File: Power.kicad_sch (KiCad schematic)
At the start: 18 parts, among them U1 LP5907MFX-1.8, U4 TLV75525PDBV, U7 LP5907MFX-1.2

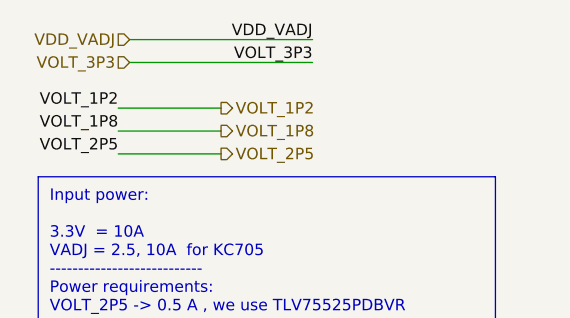
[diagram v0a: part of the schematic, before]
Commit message: DRC, ERC OK
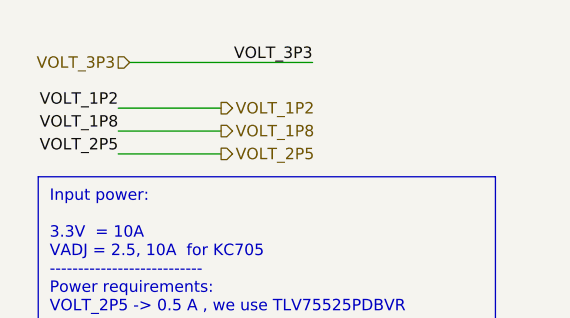
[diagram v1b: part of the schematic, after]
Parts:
- D2, D3, D4: footprint Diodes_SMD:D_SOD-523 -> SODFL1608X70N
- R16, R17, R8: symbol FMC_MIPI_v2-rescue:R-Device -> FMC_MIPI_v2:R
- U1: footprint TO_SOT_Packages_SMD:SOT-23-5 -> Package_TO_SOT_SMD:SOT-23-5; symbol FMC_MIPI_v2-rescue:LP5907MFX-1.8-Regulator_Linear -> FMC_MIPI_v2:LP5907MFX-1.8-Regulator_Linear
- U4: symbol FMC_MIPI_v2-rescue:TLV75525PDBV-Regulator_Linear -> FMC_MIPI_v2:TLV75525PDBV-Regulator_Linear
- U7: footprint TO_SOT_Packages_SMD:SOT-23-5 -> Package_TO_SOT_SMD:SOT-23-5; symbol FMC_MIPI_v2-rescue:LP5907MFX-1.2-Regulator_Linear -> FMC_MIPI_v2:LP5907MFX-1.2-Regulator_Linear
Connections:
- removed net Earth: C25.1, C26.1, C27.1, C28.1, C29.1, C30.1, C31.1, C7.1, C8.1, D2.2, D3.2, D4.2, U1.2 (GND), U4.2 (GND), U7.2 (GND)
- new net: C26.1, C31.1, D4.2
- new net: C29.1, C8.1, D2.2
- new net: C28.1, C30.1, D3.2
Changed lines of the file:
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@@
-    (stroke (width 0) (type default) (color 0 0 0 0))
-  )
-  (wire (pts (xy 45.72 13.97) (xy 25.4 13.97))
     (stroke (width 0) (type default) (color 0 0 0 0))
   )
@@
     (effects (font (size 1.27 1.27)) (justify right bottom))
   )
-  (label "VDD_VADJ" (at 45.72 13.97 180)
-    (effects (font (size 1.27 1.27)) (justify right bottom))
-  )
   (label "VOLT_1P2" (at 101.6 137.16 180)
     (effects (font (size 1.27 1.27)) (justify right bottom))
@@
     (effects (font (size 1.27 1.27)) (justify left))
   )
-  (hierarchical_label "VDD_VADJ" (shape input) (at 25.4 13.97 180)
-    (effects (font (size 1.27 1.27)) (justify right))
-  )
   (hierarchical_label "VOLT_3P3" (shape input) (at 25.4 16.51 180)
     (effects (font (size 1.27 1.27)) (justify right))
@@
       (effects (font (size 1.27 1.27)) (justify left) hide)
     )
-    (property "Footprint" "Diodes_SMD:D_SOD-523" (id 2) (at 96.52 76.2 0)
+    (property "Footprint" "SODFL1608X70N" (id 2) (at 96.52 76.2 0)
       (effects (font (size 1.27 1.27)) (justify left bottom) hide)
     )
@@
       (effects (font (size 1.27 1.27)) (justify left) hide)
     )
-    (property "Footprint" "Diodes_SMD:D_SOD-523" (id 2) (at 93.98 109.22 0)
+    (property "Footprint" "SODFL1608X70N" (id 2) (at 93.98 109.22 0)
       (effects (font (size 1.27 1.27)) (justify left bottom) hide)
     )
@@
       (effects (font (size 1.27 1.27)) (justify left) hide)
     )
-    (property "Footprint" "Diodes_SMD:D_SOD-523" (id 2) (at 93.98 147.32 0)
+    (property "Footprint" "SODFL1608X70N" (id 2) (at 93.98 147.32 0)
       (effects (font (size 1.27 1.27)) (justify left bottom) hide)
     )
@@
     (pin "2")
   )
-  (symbol (lib_id "FMC_MIPI_v2-rescue:Earth-power") (at 54.61 80.01 0) (unit 1)
+  (symbol (lib_id "FMC_MIPI_v2:Earth") (at 54.61 80.01 0) (unit 1)
     (in_bom yes) (on_board yes)
     (property "Reference" "#PWR0149" (id 0) (at 54.61 86.36 0)
@@
     (pin "2")
   )
-  (symbol (lib_id "FMC_MIPI_v2-rescue:Earth-power") (at 34.29 80.01 0) (unit 1)
+  (symbol (lib_id "FMC_MIPI_v2:Earth") (at 34.29 80.01 0) (unit 1)
     (in_bom yes) (on_board yes)
     (property "Reference" "#PWR0150" (id 0) (at 34.29 86.36 0)
@@
     (pin "1")
   )
-  (symbol (lib_id "FMC_MIPI_v2-rescue:Earth-power") (at 68.58 83.82 0) (unit 1)
+  (symbol (lib_id "FMC_MIPI_v2:Earth") (at 68.58 83.82 0) (unit 1)
     (in_bom yes) (on_board yes)
     (property "Reference" "#PWR0151" (id 0) (at 68.58 90.17 0)
@@
     (pin "1")
   )
-  (symbol (lib_id "FMC_MIPI_v2-rescue:R-Device") (at 39.37 72.39 0) (mirror y) (unit 1)
+  (symbol (lib_id "FMC_MIPI_v2:R") (at 39.37 72.39 0) (mirror y) (unit 1)
     (in_bom yes) (on_board yes)
     (property "Reference" "R16" (id 0) (at 41.91 72.39 90))
@@
     (pin "2")
   )
-  (symbol (lib_id "FMC_MIPI_v2-rescue:TLV75525PDBV-Regulator_Linear") (at 54.61 68.58 0) (unit 1)
+  (symbol (lib_id "FMC_MIPI_v2:TLV75525PDBV-Regulator_Linear") (at 54.61 68.58 0) (unit 1)
     (in_bom yes) (on_board yes)
     (property "Reference" "U4" (id 0) (at 54.61 59.8932 0))
@@
     (pin "5")
   )
-  (symbol (lib_id "FMC_MIPI_v2-rescue:LP5907MFX-1.8-Regulator_Linear") (at 54.61 101.6 0) (unit 1)
+  (symbol (lib_id "FMC_MIPI_v2:LP5907MFX-1.8-Regulator_Linear") (at 54.61 101.6 0) (unit 1)
     (in_bom yes) (on_board yes)
     (property "Reference" "U1" (id 0) (at 54.61 92.2782 0))
     (property "Value" "LP5907MFX-1.8" (id 1) (at 54.61 94.5896 0))
-    (property "Footprint" "TO_SOT_Packages_SMD:SOT-23-5" (id 2) (at 54.61 92.71 0)
+    (property "Footprint" "Package_TO_SOT_SMD:SOT-23-5" (id 2) (at 54.61 92.71 0)
       (effects (font (size 1.27 1.27)) hide)
     )
@@
     (pin "5")
   )
-  (symbol (lib_id "FMC_MIPI_v2-rescue:Earth-power") (at 54.61 113.03 0) (unit 1)
+  (symbol (lib_id "FMC_MIPI_v2:Earth") (at 54.61 113.03 0) (unit 1)
     (in_bom yes) (on_board yes)
     (property "Reference" "#PWR0134" (id 0) (at 54.61 119.38 0)
@@
     (pin "2")
   )
-  (symbol (lib_id "FMC_MIPI_v2-rescue:Earth-power") (at 34.29 113.03 0) (unit 1)
+  (symbol (lib_id "FMC_MIPI_v2:Earth") (at 34.29 113.03 0) (unit 1)
     (in_bom yes) (on_board yes)
     (property "Reference" "#PWR0135" (id 0) (at 34.29 119.38 0)
@@
     (pin "1")
   )
-  (symbol (lib_id "FMC_MIPI_v2-rescue:Earth-power") (at 68.58 116.84 0) (unit 1)
+  (symbol (lib_id "FMC_MIPI_v2:Earth") (at 68.58 116.84 0) (unit 1)
     (in_bom yes) (on_board yes)
     (property "Reference" "#PWR0136" (id 0) (at 68.58 123.19 0)
@@
     (pin "1")
   )
-  (symbol (lib_id "FMC_MIPI_v2-rescue:R-Device") (at 39.37 105.41 0) (mirror y) (unit 1)
+  (symbol (lib_id "FMC_MIPI_v2:R") (at 39.37 105.41 0) (mirror y) (unit 1)
     (in_bom yes) (on_board yes)
     (property "Reference" "R8" (id 0) (at 41.91 105.41 90))
@@
     (pin "2")
   )
-  (symbol (lib_id "FMC_MIPI_v2-rescue:LP5907MFX-1.2-Regulator_Linear") (at 54.61 139.7 0) (unit 1)
+  (symbol (lib_id "FMC_MIPI_v2:LP5907MFX-1.2-Regulator_Linear") (at 54.61 139.7 0) (unit 1)
     (in_bom yes) (on_board yes)
     (property "Reference" "U7" (id 0) (at 54.61 130.3782 0))
     (property "Value" "LP5907MFX-1.2" (id 1) (at 54.61 132.6896 0))
-    (property "Footprint" "TO_SOT_Packages_SMD:SOT-23-5" (id 2) (at 54.61 130.81 0)
+    (property "Footprint" "Package_TO_SOT_SMD:SOT-23-5" (id 2) (at 54.61 130.81 0)
       (effects (font (size 1.27 1.27)) hide)
     )
@@
     (pin "5")
   )
-  (symbol (lib_id "FMC_MIPI_v2-rescue:Earth-power") (at 54.61 152.4 0) (unit 1)
+  (symbol (lib_id "FMC_MIPI_v2:Earth") (at 54.61 152.4 0) (unit 1)
     (in_bom yes) (on_board yes)
     (property "Reference" "#PWR0152" (id 0) (at 54.61 158.75 0)
@@
     (pin "2")
   )
-  (symbol (lib_id "FMC_MIPI_v2-rescue:Earth-power") (at 34.29 151.13 0) (unit 1)
+  (symbol (lib_id "FMC_MIPI_v2:Earth") (at 34.29 151.13 0) (unit 1)
     (in_bom yes) (on_board yes)
     (property "Reference" "#PWR0153" (id 0) (at 34.29 157.48 0)
@@
     (pin "1")
   )
-  (symbol (lib_id "FMC_MIPI_v2-rescue:Earth-power") (at 68.58 154.94 0) (unit 1)
+  (symbol (lib_id "FMC_MIPI_v2:Earth") (at 68.58 154.94 0) (unit 1)
     (in_bom yes) (on_board yes)
     (property "Reference" "#PWR0154" (id 0) (at 68.58 161.29 0)
@@
     (pin "1")
   )
-  (symbol (lib_id "FMC_MIPI_v2-rescue:R-Device") (at 39.37 143.51 0) (mirror y) (unit 1)
+  (symbol (lib_id "FMC_MIPI_v2:R") (at 39.37 143.51 0) (mirror y) (unit 1)
     (in_bom yes) (on_board yes)
     (property "Reference" "R17" (id 0) (at 41.91 143.51 90))

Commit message: All warnings fixed
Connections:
- net Earth: now reaches C26.1, C31.1, D4.2
- net Earth: now also C25.1, C27.1, C28.1, C29.1, C30.1, C7.1, C8.1, D2.2, D3.2, U1.2 (GND), U4.2 (GND), U7.2 (GND)

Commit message: JLCPCB BOM OK
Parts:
- C29: LCSC (none) -> C1779; Part Number C2012X7R1H475K125AC -> CL21A475KAQNNNE
- C7: LCSC (none) -> C28323; Part Number UMK212B7105KG-T -> CL21B105KBFNNNE
- D2, D3, D4: LCSC (none) -> C117557
- R16, R17, R8: LCSC (none) -> C17477; Part Number RC0805JR-070RL -> 0805W8F0000T5E
- U1: LCSC (none) -> C92498; Part Number (none) -> LP5907MFX-1.8/NOPB; Part number LP5907MFX-1.8/NOPB -> (none)
- U4: LCSC (none) -> NeedToAsk
- U7: LCSC (none) -> C73478
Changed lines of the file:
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@@
       (effects (font (size 1.27 1.27)) (justify left bottom) hide)
+    )
+    (property "LCSC" "C117557" (id 10) (at 92.71 66.04 90)
+      (effects (font (size 1.27 1.27)) hide)
     )
     (pin "1")
@@
       (effects (font (size 1.27 1.27)) (justify left bottom) hide)
     )
+    (property "LCSC" "C117557" (id 10) (at 90.17 99.06 90)
+      (effects (font (size 1.27 1.27)) hide)
+    )
     (pin "1")
     (pin "2")
@@
       (effects (font (size 1.27 1.27)) hide)
     )
-    (property "Datasheet" "https://www.mouser.com/ProductDetail/TDK/C2012X7R1H475K125AC?qs=P1JMDcb91o6brNyz9C%252BI3w%3D%3D" (id 3) (at 80.01 104.14 0)
-      (effects (font (size 1.27 1.27)) hide)
-    )
-    (property "Part Number" "C2012X7R1H475K125AC" (id 4) (at 80.01 104.14 0)
+    (property "Datasheet" "https://www.mouser.com/ProductDetail/Samsung-Electro-Mechanics/CL21A475KAQNNNE?qs=yOVawPpwOwkWIBpK%2Fbg0Aw%3D%3D" (id 3) (at 80.01 104.14 0)
+      (effects (font (size 1.27 1.27)) hide)
+    )
+    (property "Part Number" "CL21A475KAQNNNE" (id 4) (at 80.01 104.14 0)
       (effects (font (size 1.27 1.27)) hide)
     )
@@
     )
     (property "Voltage" "25V" (id 6) (at 80.01 104.14 0)
+      (effects (font (size 1.27 1.27)) hide)
+    )
+    (property "LCSC" "C1779" (id 7) (at 80.01 104.14 0)
       (effects (font (size 1.27 1.27)) hide)
     )
@@
     (property "Manufacturer_Part_Number" "UCLAMP0501H.TCT" (id 9) (at 76.2 147.32 0)
       (effects (font (size 1.27 1.27)) (justify left bottom) hide)
+    )
+    (property "LCSC" "C117557" (id 10) (at 90.17 137.16 90)
+      (effects (font (size 1.27 1.27)) hide)
     )
     (pin "1")
@@
       (effects (font (size 1.27 1.27)) hide)
     )
-    (property "Datasheet" "https://www.mouser.com/ProductDetail/YAGEO/RC0805JR-070RL?qs=3ldFlDWnkKyEhdaPjQHEFA%3D%3D" (id 3) (at 39.37 72.39 0)
+    (property "Datasheet" "https://www.mouser.com/ProductDetail/Royalohm/0805W8F0000T5E?qs=e8oIoAS2J1TZ0ecBNS6tzg%3D%3D" (id 3) (at 39.37 72.39 0)
       (effects (font (size 1.27 1.27)) hide)
     )
@@
       (effects (font (size 1.524 1.524)) hide)
     )
-    (property "Part Number" "RC0805JR-070RL" (id 6) (at 39.37 72.39 90)
-      (effects (font (size 1.524 1.524)) hide)
+    (property "Part Number" "0805W8F0000T5E" (id 6) (at 39.37 72.39 90)
+      (effects (font (size 1.524 1.524)) hide)
+    )
+    (property "LCSC" "C17477" (id 7) (at 388.62 198.12 90)
+      (effects (font (size 1.27 1.27)) hide)
     )
     (pin "1")
@@
       (effects (font (size 1.27 1.27)) hide)
     )
+    (property "LCSC" "NeedToAsk" (id 4) (at 54.61 68.58 0)
+      (effects (font (size 1.27 1.27)) hide)
+    )
     (pin "1")
     (pin "2")
@@
       (effects (font (size 1.27 1.27)) hide)
     )
-    (property "Part number" "LP5907MFX-1.8/NOPB" (id 4) (at 54.61 101.6 0)
+    (property "Part Number" "LP5907MFX-1.8/NOPB" (id 4) (at 54.61 101.6 0)
+      (effects (font (size 1.27 1.27)) hide)
+    )
+    (property "LCSC" "C92498" (id 5) (at 54.61 101.6 0)
       (effects (font (size 1.27 1.27)) hide)
     )
@@
       (effects (font (size 1.27 1.27)) hide)
     )
-    (property "Datasheet" "https://www.mouser.com/ProductDetail/Taiyo-Yuden/UMK212B7105KG-T?qs=PzICbMaShUdi76GLXMVYcA%3D%3D" (id 3) (at 34.29 106.68 0)
-      (effects (font (size 1.27 1.27)) hide)
-    )
-    (property "Part Number" "UMK212B7105KG-T" (id 4) (at 34.29 106.68 0)
+    (property "Datasheet" "https://www.mouser.com/ProductDetail/Samsung-Electro-Mechanics/CL21B105KBFNNNE?qs=yOVawPpwOwmddQEBPU6Y9A%3D%3D" (id 3) (at 34.29 106.68 0)
+      (effects (font (size 1.27 1.27)) hide)
+    )
+    (property "Part Number" "CL21B105KBFNNNE" (id 4) (at 34.29 106.68 0)
       (effects (font (size 1.27 1.27)) hide)
     )
@@
     )
     (property "Voltage" "50 VDC" (id 6) (at 34.29 106.68 0)
+      (effects (font (size 1.27 1.27)) hide)
+    )
+    (property "LCSC" "C28323" (id 7) (at 34.29 106.68 0)
       (effects (font (size 1.27 1.27)) hide)
     )
@@
       (effects (font (size 1.27 1.27)) hide)
     )
-    (property "Datasheet" "https://www.mouser.com/ProductDetail/YAGEO/RC0805JR-070RL?qs=3ldFlDWnkKyEhdaPjQHEFA%3D%3D" (id 3) (at 39.37 105.41 0)
+    (property "Datasheet" "https://www.mouser.com/ProductDetail/Royalohm/0805W8F0000T5E?qs=e8oIoAS2J1TZ0ecBNS6tzg%3D%3D" (id 3) (at 39.37 105.41 0)
       (effects (font (size 1.27 1.27)) hide)
     )
@@
       (effects (font (size 1.524 1.524)) hide)
     )
-    (property "Part Number" "RC0805JR-070RL" (id 6) (at 39.37 105.41 90)
-      (effects (font (size 1.524 1.524)) hide)
+    (property "Part Number" "0805W8F0000T5E" (id 6) (at 39.37 105.41 90)
+      (effects (font (size 1.524 1.524)) hide)
+    )
+    (property "LCSC" "C17477" (id 7) (at 388.62 198.12 90)
+      (effects (font (size 1.27 1.27)) hide)
     )
     (pin "1")
@@
       (effects (font (size 1.27 1.27)) hide)
     )
+    (property "LCSC" "C73478" (id 4) (at 54.61 139.7 0)
+      (effects (font (size 1.27 1.27)) hide)
+    )
     (pin "1")
     (pin "2")
@@
       (effects (font (size 1.27 1.27)) hide)
     )
-    (property "Datasheet" "https://www.mouser.com/ProductDetail/YAGEO/RC0805JR-070RL?qs=3ldFlDWnkKyEhdaPjQHEFA%3D%3D" (id 3) (at 39.37 143.51 0)
+    (property "Datasheet" "https://www.mouser.com/ProductDetail/Royalohm/0805W8F0000T5E?qs=e8oIoAS2J1TZ0ecBNS6tzg%3D%3D" (id 3) (at 39.37 143.51 0)
       (effects (font (size 1.27 1.27)) hide)
     )
@@
       (effects (font (size 1.524 1.524)) hide)
     )
-    (property "Part Number" "RC0805JR-070RL" (id 6) (at 39.37 143.51 90)
-      (effects (font (size 1.524 1.524)) hide)
-    )
-    (pin "1")
+    (property "Part Number" "0805W8F0000T5E" (id 6) (at 39.37 143.51 90)
+      (effects (font (size 1.524 1.524)) hide)
+    )
+    (property "LCSC" "C17477" (id 7) (at 388.62 198.12 90)
+      (effects (font (size 1.27 1.27)) hide)
+    )
+    (pin "1")

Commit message: Generated BOM, before Gerbers generation
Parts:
- U4: LCSC NeedToAsk -> C2867155
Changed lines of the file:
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@@
       (effects (font (size 1.27 1.27)) hide)
     )
-    (property "LCSC" "NeedToAsk" (id 4) (at 54.61 68.58 0)
+    (property "LCSC" "C2867155" (id 4) (at 54.61 68.58 0)
       (effects (font (size 1.27 1.27)) hide)
     )
